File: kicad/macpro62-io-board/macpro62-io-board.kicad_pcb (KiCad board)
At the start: 6 copper layers, 101 x 173.6 mm, 113 parts, among them J1 IOB-HS1 MCIO 124 RA <- CB J3 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, J11 C1 GPU DP L0 (4-lane), J12 C2 GPU DP L1 (4-lane), J13 C3 GPU DP L3 (2-lane), J14 C4 GPU DP L4 (2-lane), J15 C5 iGPU DDI-B, J16 C6 iGPU DDI-C, J2 DISPLAY-LINK MCIO 74 RA <- Fa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, J21 USB-A A1 10G, J22 USB-A A2 10G, J23 USB-A A3 10G, J24 USB-A A4 10G, J25 ETH1 i226-V 2.5GbE (roomy fra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, J26 ETH2 rev B AQC107 10GbE (DNP 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, J27 HDMI (GPU link 2 via TDP158), J28 Stock audio module connector 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, J29 Speaker 2P (stock lead; pitch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, J3 Stock PSU DC-out 12P (UNCONFI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, J30 Optional stock/remote power b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, J31 I/O-wall (821-2222) flex ZIF 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, J4 Stock PSU signal 6P (UNCONFIR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, J5 PSU pass-through -> BP J2 (12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, J6 IOB-LINK GH15 <- BP J6, SW1 Power button on the IOB behin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, SW2 DIAG button, U1 TPS65994AD PD #1 (C1, C2), U11 TUSB1046A C1 alt-mode mux/red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, U12 TUSB1046A C2 alt-mode mux/red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, U13 TUSB1046A C3 alt-mode mux/red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, U14 TUSB1046A C4 alt-mode mux/red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, U15 TUSB1046A C5 alt-mode mux/red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, U16 TUSB1046A C6 alt-mode mux/red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, U2 TPS65994AD PD #2 (C3, C4), U21 TUSB1002A A1 10G redriver, U22 TUSB1002A A2 10G redriver, U23 TUSB1002A A3 10G redriver, U24 TUSB1002A A4 10G redriver, U25 USB-A A1 VBUS switch 1.5 A (S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, U26 USB-A A2 VBUS switch 1.5 A (S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, U27 USB-A A3 VBUS switch 1.5 A (S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, U28 USB-A A4 VBUS switch 1.5 A (S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, U3 TPS65994AD PD #3 (C5, C6), U30 Hall A (DRV5032 class) - posi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, U31 Hall B (DRV5032 class) - posi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, U32 CH334R hub H1b (C4-C6 + codec), U33 CH334R hub H2 (A1-A4) <- IOB-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, U34 CH334R hub H1a (C1-C3 + H1b) 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, U4 PD #1 config SPI flash (W25Q8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, U40 TPS259824ON eFuse 12 V in (15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, U41 TPS56C215 5V_C buck (USB-C VB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, U42 TPS56C215 5V_A buck (USB-A VB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, U43 TLV62585 3V3 (3 A) from 5V_SYS, U50 i226-V 2.5GbE (PCIe x1 from H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, U51 i226-V NVM SPI flash (size pe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, U6 PD #2 config SPI flash, U60 TDP158 HDMI 2.0 retimer (GPU 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, U61 1V1 LDO (TDP158 core), U7 PD #3 config SPI flash, U70 C-Media CM108B USB audio code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, U71 PAM8302A mono class-D 2.5 W (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, U80 TLC59116 16-ch I2C LED driver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, U81 LIS2DH12 accelerometer (rotat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, U82 BL24C64A IOB ID EEPROM @0x51, U83 TCA9517 I2C buffer (I2C_SYS <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, U84 74LVC1G07 PD_INT -> IOB_INT_N, Y1 12 MHz hub crystal, Y2 12 MHz hub crystal, Y3 12 MHz hub crystal, Y4 25 MHz (i226-V), Y5 12 MHz (CM108B)

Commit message: I/O board: second 2.5GbE (2x i226-V, HR913790A set back), ETH2 plate opening, CPU link pinout v0.2
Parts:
- added L45: i226 #2 SVR inductor, MP62_IO:L_1008_2520Metric, B.Cu at (113.0, 101.5)
- added U52: i226-V #2 2.5GbE (PCIe x1 from HS1 k14, PCH RP4), MP62_IO:MP62_Intel_i226V_QFN-56_7x7_P0.4_PLACEHOLDER, B.Cu at (113.0, 108.0)
- added U53: i226-V #2 NVM SPI flash, MP62_IO:SOIC-8_3.9x4.9mm_P1.27mm, B.Cu at (121.5, 113.5)
- added Y6: 25 MHz (i226-V #2), MP62_IO:Crystal_SMD_3225-4Pin_3.2x2.5mm, B.Cu at (113.0, 115.0)
- J25: value ETH1 i226-V 2.5GbE (roomy frame side) -> ETH1 i226-V #1 2.5GbE, HR913790A (face behind the frame plane); footprint MP62_IO:MP62_RJ45_Mag_2G5_Vertical_PLACEHOLDER -> MP62_IO:MP62_RJ45_HanRun_HR913790A_Vertical_2G5
- J26: value ETH2 rev B AQC107 10GbE (DNP rev A; frame slot 15.6: jack set back) -> ETH2 i226-V #2 2.5GbE, HR913790A; H-side frame slot 15.6 x 13.0 < body 16.2 x 17.0: jack set back behind the frame, plu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; footprint MP62_IO:MP62_RJ45_Mag_2G5_Vertical_PLACEHOLDER -> MP62_IO:MP62_RJ45_HanRun_HR913790A_Vertical_2G5
- moved Y2 6.52 mm to (88.0, 104.5)

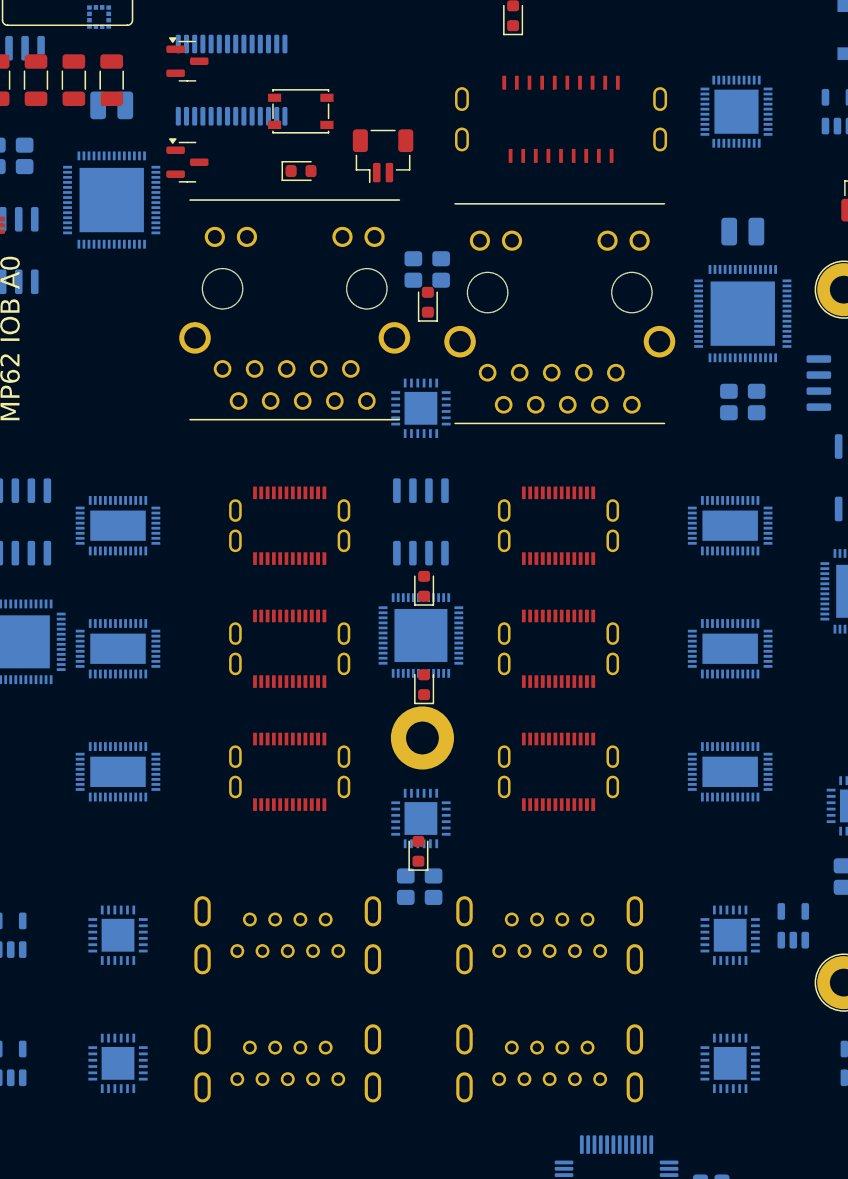
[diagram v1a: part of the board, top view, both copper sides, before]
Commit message: I/O plate: flex retraced from flat scan, flush inner face, LED pockets, measured 16.5-18 mm gap; connector re-grid
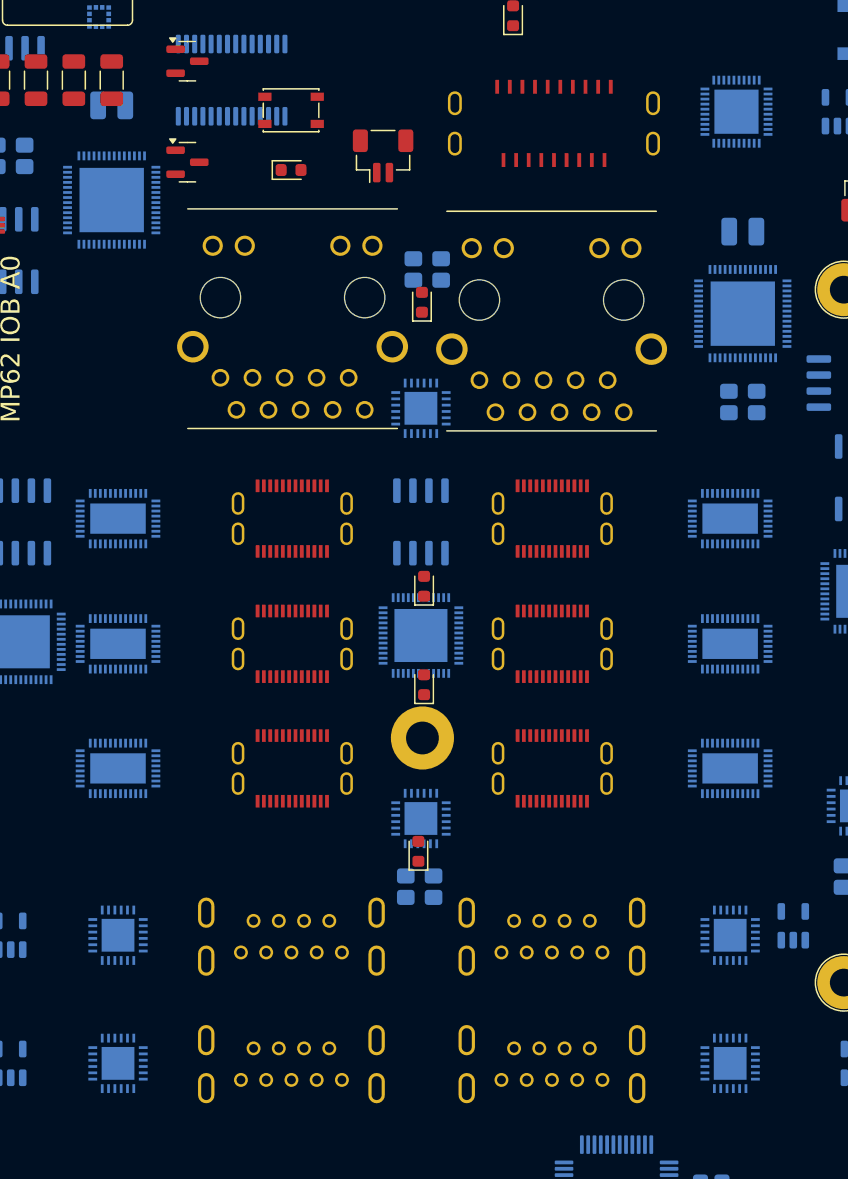
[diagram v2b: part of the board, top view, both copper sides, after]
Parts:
- D20: value Power/sleep LED (white) under button cap -> DNP with the stock flex (its 2 button LEDs light the cap via J31); power/sleep LED only without the flex
- D21: value Light-pipe LED: HDMI label -> Light-pipe LED: HDMI label - DNP with the stock flex (its own LEDs light the icon pads via J31)
- D22: value Light-pipe LED: ETH icon -> Light-pipe LED: ETH icon - DNP with the stock flex (its own LEDs light the icon pads via J31)
- D23: value Light-pipe LED: USB-C icon upper -> Light-pipe LED: USB-C icon upper - DNP with the stock flex (its own LEDs light the icon pads via J31)
- D24: value Light-pipe LED: USB-C icon lower -> Light-pipe LED: USB-C icon lower - DNP with the stock flex (its own LEDs light the icon pads via J31)
- D25: value Light-pipe LED: USB icon -> Light-pipe LED: USB icon - DNP with the stock flex (its own LEDs light the icon pads via J31)
- D26: value Light-pipe LED: audio icons -> Light-pipe LED: audio icons - DNP with the stock flex (its own LEDs light the icon pads via J31)
- J11: value C1 GPU DP L0 (4-lane) -> C1 GPU DP L0 (4-lane); FG-ST-C-24P-VT-SMT-15.0 C51911913 H15.0 on +2.9 port riser (mouth 17.90)
- J12: value C2 GPU DP L1 (4-lane) -> C2 GPU DP L1 (4-lane); FG-ST-C-24P-VT-SMT-15.0 C51911913 H15.0 on +2.9 port riser (mouth 17.90)
- J13: value C3 GPU DP L3 (2-lane) -> C3 GPU DP L3 (2-lane); FG-ST-C-24P-VT-SMT-15.0 C51911913 H15.0 on +2.9 port riser (mouth 17.90)
- J14: value C4 GPU DP L4 (2-lane) -> C4 GPU DP L4 (2-lane); FG-ST-C-24P-VT-SMT-15.0 C51911913 H15.0 on +2.8 port riser (mouth 17.82)
- J15: value C5 iGPU DDI-B -> C5 iGPU DDI-B; FG-ST-C-24P-VT-SMT-15.0 C51911913 H15.0 on +2.8 port riser (mouth 17.82)
- J16: value C6 iGPU DDI-C -> C6 iGPU DDI-C; FG-ST-C-24P-VT-SMT-15.0 C51911913 H15.0 on +2.8 port riser (mouth 17.82)
- J21: value USB-A A1 10G -> USB-A A1 10G; KH-3.0AF180WJ-15JB C2979045 L15.0 on +2.5 port riser (mouth 17.49)
- J22: value USB-A A2 10G -> USB-A A2 10G; KH-3.0AF180WJ-15JB C2979045 L15.0 on +2.5 port riser (mouth 17.49)
- J23: value USB-A A3 10G -> USB-A A3 10G; KH-3.0AF180WJ-15JB C2979045 L15.0 on +2.4 port riser (mouth 17.38)
- J24: value USB-A A4 10G -> USB-A A4 10G; KH-3.0AF180WJ-15JB C2979045 L15.0 on +2.4 port riser (mouth 17.38)
- J25: value ETH1 i226-V #1 2.5GbE, HR913790A (face behind the frame plane) -> ETH1 i226-V #1 2.5GbE. HR913790A (16.9) TOO TALL for D0 18: face must be <= 13.6 -> non-magnetic vertical RJ45 <= 13.0 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
- J26: value ETH2 i226-V #2 2.5GbE, HR913790A; H-side frame slot 15.6 x 13.0 < body 16.2 x 17.0: jack set back behind the frame, plu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 -> ETH2 i226-V #2 2.5GbE. HR913790A (16.9) TOO TALL for D0 18: face must be <= 13.7 (behind the frame) -> non-magnetic ver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
- J27: value HDMI (GPU link 2 via TDP158) -> HDMI (GPU link 2 via TDP158); vertical H15 (JLC C9900153431, verify shell <= 15.4 x 5.6) on +2.2 port riser (mouth 17.2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
- SW1: value Power button on the IOB behind the plate opening (printed cap); stock button is NOT on the stock IOB -> DNP with the stock 821-2222-A flex (its dome switch is the power button, via J31); fit only without the flex
- moved J26 0.88 mm to (97.9, 108.6)
- moved D20 0.79 mm to (77.2, 96.6)
- moved SW1 0.77 mm to (77.2, 91.9)
- moved J11 0.74 mm to (97.9, 124.2)
- moved J25 0.72 mm to (77.3, 108.4)
- moved J27 0.65 mm to (98.0, 92.9)
- moved J12 0.63 mm to (97.9, 134.2)
- moved J14 0.60 mm to (77.3, 124.2)
- moved U11 0.56 mm to (112.0, 124.2)
- moved U14 0.56 mm to (63.5, 124.2)
- moved J13 0.56 mm to (97.9, 144.0)
- moved D22 0.47 mm to (87.6, 107.1)
- moved J15 0.44 mm to (77.3, 134.2)
- moved U12 0.39 mm to (112.0, 134.2)
- moved U15 0.39 mm to (63.5, 134.2)
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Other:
- board text added: "All ports are VERTICAL (mating axis normal to the board); the plate is curved with no lands (stock flex must lie flat), mouths flush at the outboard edge (plan 4.4/4.7)."
- board text added: "D0 = 18.0 crown / 16.5 edge: USB-C/USB-A/HDMI need 17.2-17.9 board-to-mouth -> port risers (+2.2..2.9) under 15.0 parts; RJ45 face <= 13.6 (plan 4.7.4)."
- board text added: "Port grid (stock flex cut-outs, scan 2026-10-02): USB-C Xb 43.09 / 63.69, Y 75.76 / 65.84 / 55.97; USB-A 43.12 / 63.76, Y 42.64 / 32.54; RJ45 (43.15,91.41)/(63.67,91.60); HDMI (42.96,107.07); button (63.79,108.11)."
- board text removed: "All ports are VERTICAL (mating axis normal to the board) like stock; plate openings follow the connectors; tilt (~1-3 deg est.) is taken up by the plate (plan 4.4)."
- board text removed: "Port grid: columns Xb 42.6 / 63.9; USB-C rows Y 75.2 / 65.45 / 55.7; USB-A rows 42.75 / 32.6; RJ45 Y ~92; HDMI (42.4,107.4); button (63.0,108.0)."

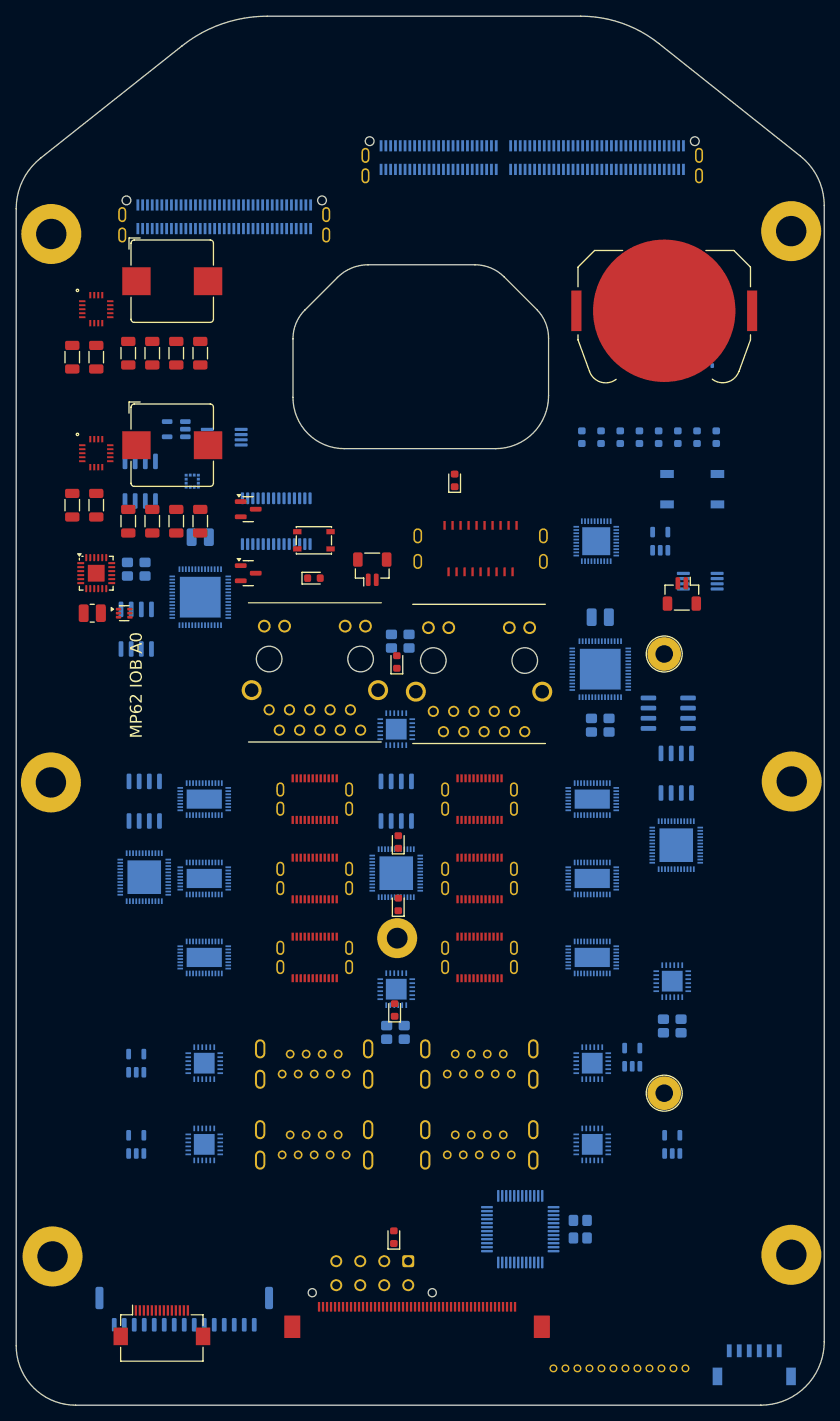
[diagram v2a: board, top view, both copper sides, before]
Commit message: I/O: tilted port risers (USB-C/USB-A/HDMI, DF40 + flex jumpers), low RJ45 + V24P05S magnetics, fan+AirPort CONN_C at stock position, ASM1182e lane share; plate R=111
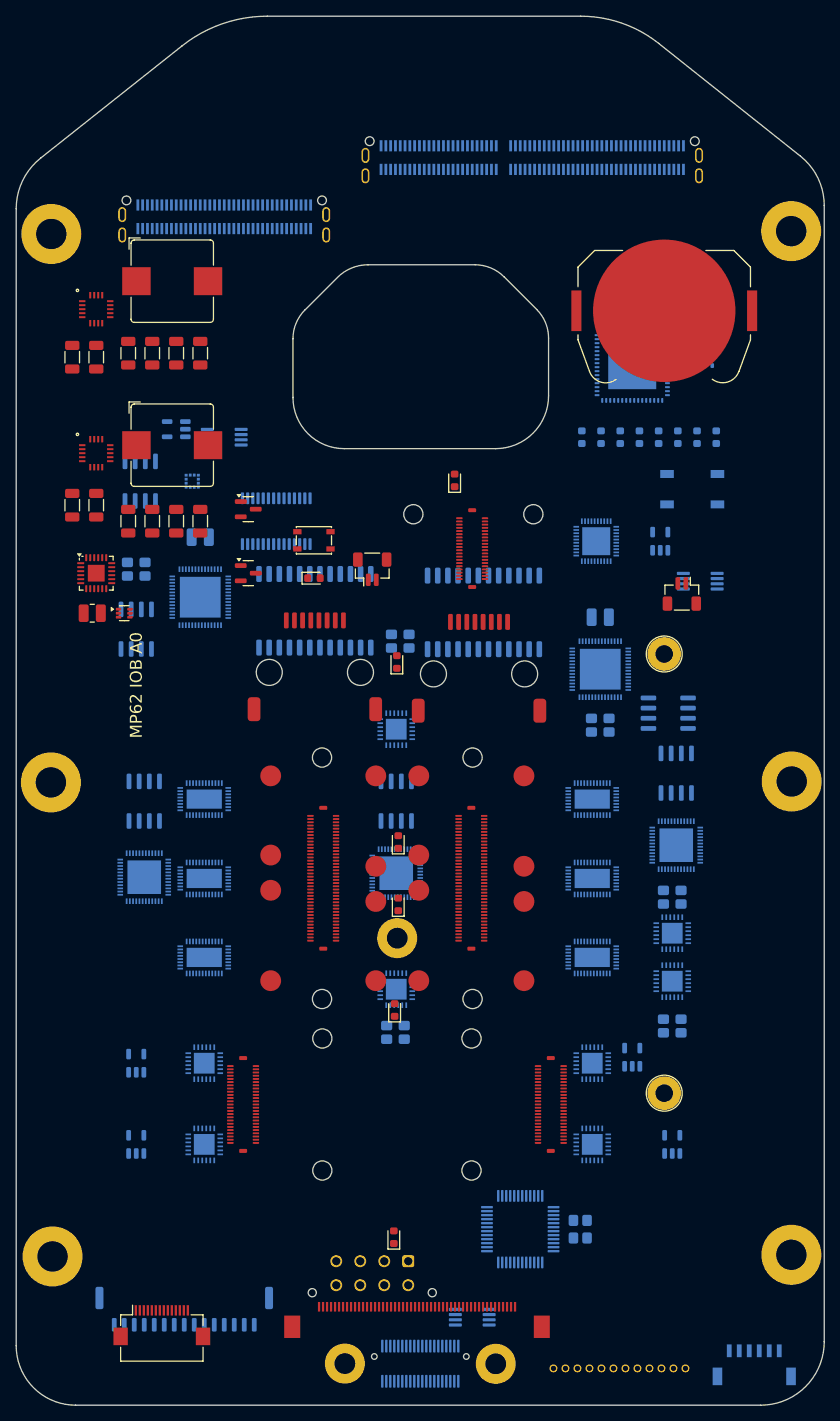
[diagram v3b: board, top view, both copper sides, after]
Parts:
- removed J11: C1 GPU DP L0 (4-lane); FG-ST-C-24P-VT-SMT-15.0 C51911913 H1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, MP62_IO:MP62_USB_C_24P_Vertical_PLACEHOLDER
- removed J12: C2 GPU DP L1 (4-lane); FG-ST-C-24P-VT-SMT-15.0 C51911913 H1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, MP62_IO:MP62_USB_C_24P_Vertical_PLACEHOLDER
- removed J13: C3 GPU DP L3 (2-lane); FG-ST-C-24P-VT-SMT-15.0 C51911913 H1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, MP62_IO:MP62_USB_C_24P_Vertical_PLACEHOLDER
- removed J14: C4 GPU DP L4 (2-lane); FG-ST-C-24P-VT-SMT-15.0 C51911913 H1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, MP62_IO:MP62_USB_C_24P_Vertical_PLACEHOLDER
- removed J15: C5 iGPU DDI-B; FG-ST-C-24P-VT-SMT-15.0 C51911913 H15.0 on +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, MP62_IO:MP62_USB_C_24P_Vertical_PLACEHOLDER
- removed J16: C6 iGPU DDI-C; FG-ST-C-24P-VT-SMT-15.0 C51911913 H15.0 on +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, MP62_IO:MP62_USB_C_24P_Vertical_PLACEHOLDER
- removed J21: USB-A A1 10G; KH-3.0AF180WJ-15JB C2979045 L15.0 on +2.5 por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, MP62_IO:MP62_USB_A3_9P_Vertical_PLACEHOLDER
- removed J22: USB-A A2 10G; KH-3.0AF180WJ-15JB C2979045 L15.0 on +2.5 por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, MP62_IO:MP62_USB_A3_9P_Vertical_PLACEHOLDER
- removed J23: USB-A A3 10G; KH-3.0AF180WJ-15JB C2979045 L15.0 on +2.4 por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, MP62_IO:MP62_USB_A3_9P_Vertical_PLACEHOLDER
- removed J24: USB-A A4 10G; KH-3.0AF180WJ-15JB C2979045 L15.0 on +2.4 por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, MP62_IO:MP62_USB_A3_9P_Vertical_PLACEHOLDER
- removed J27: HDMI (GPU link 2 via TDP158); vertical H15 (JLC C9900153431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, MP62_IO:MP62_HDMI_A_Vertical_PLACEHOLDER
- added H14: CONN_C threaded standoff (stock position 41.06, 5.17; threa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, MP62_IO:MP62_Frame_Standoff_M2_SMT_PLACEHOLDER, B.Cu at (99.9, 194.8)
- added H15: CONN_C threaded standoff (stock position 59.92, 5.20; threa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, MP62_IO:MP62_Frame_Standoff_M2_SMT_PLACEHOLDER, B.Cu at (81.1, 194.8)
- added H21: RC_H cradle M2 screw (printed PA12 wedge cradle), MP62_IO:MP62_Cradle_Screw_M2_NPTH, F.Cu at (97.0, 149.2)
- added H22: RC_H cradle M2 screw (printed PA12 wedge cradle), MP62_IO:MP62_Cradle_Screw_M2_NPTH, F.Cu at (97.0, 119.0)
- added H23: RC_O cradle M2 screw (printed PA12 wedge cradle), MP62_IO:MP62_Cradle_Screw_M2_NPTH, F.Cu at (78.2, 149.2)
- added H24: RC_O cradle M2 screw (printed PA12 wedge cradle), MP62_IO:MP62_Cradle_Screw_M2_NPTH, F.Cu at (78.2, 119.0)
- added H25: RA_H cradle M2 screw (printed PA12 wedge cradle), MP62_IO:MP62_Cradle_Screw_M2_NPTH, F.Cu at (96.9, 170.7)
- added H26: RA_H cradle M2 screw (printed PA12 wedge cradle), MP62_IO:MP62_Cradle_Screw_M2_NPTH, F.Cu at (96.9, 154.2)
- added H27: RA_O cradle M2 screw (printed PA12 wedge cradle), MP62_IO:MP62_Cradle_Screw_M2_NPTH, F.Cu at (78.3, 170.7)
- added H28: RA_O cradle M2 screw (printed PA12 wedge cradle), MP62_IO:MP62_Cradle_Screw_M2_NPTH, F.Cu at (78.3, 154.2)
- added H29: RH cradle M2 screw (printed PA12 wedge cradle), MP62_IO:MP62_Cradle_Screw_M2_NPTH, F.Cu at (104.6, 88.6)
- added H30: RH cradle M2 screw (printed PA12 wedge cradle), MP62_IO:MP62_Cradle_Screw_M2_NPTH, F.Cu at (89.6, 88.6)
- added J7: CONN_C fan + AirPort 2x20 @0.5 (stock press B2B). DF12-40DS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, MP62_IO:MP62_Hirose_DF12-40DS-0.5V_PLACEHOLDER, B.Cu at (90.5, 194.8)
- added JR1: RC_H riser link (C, ports C1/C2/C3, tilt -5.27 deg): DF40C-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, MP62_IO:MP62_Hirose_DF40C-80DS-0.4V_PLACEHOLDER, F.Cu at (96.9, 134.1)
- added JR2: RC_O riser link (C, ports C4/C5/C6, tilt 5.47 deg): DF40C-8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, MP62_IO:MP62_Hirose_DF40C-80DS-0.4V_PLACEHOLDER, F.Cu at (78.4, 134.1)
- added JR3: RA_H riser link (A, ports A1/A2, tilt -5.25 deg): DF40C-50D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, MP62_IO:MP62_Hirose_DF40C-50DS-0.4V_PLACEHOLDER, F.Cu at (106.8, 162.4)
- added JR4: RA_O riser link (A, ports A3/A4, tilt 5.51 deg): DF40C-50DS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, MP62_IO:MP62_Hirose_DF40C-50DS-0.4V_PLACEHOLDER, F.Cu at (68.4, 162.4)
- added JR5: RH riser link (HDMI, ports HDMI, tilt -5.33 deg): DF40C-40D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, MP62_IO:MP62_Hirose_DF40C-40DS-0.4V_PLACEHOLDER, F.Cu at (97.0, 92.9)
- added PG1: RC_H pogo VBUS_C3, working height 5.94, MP62_IO:MP62_Pogo_SMD_D2.0_PLACEHOLDER, F.Cu at (103.5, 146.9)
- added PG10: RC_O pogo VBUS_C3, working height 7.14, MP62_IO:MP62_Pogo_SMD_D2.0_PLACEHOLDER, F.Cu at (84.9, 121.3)
- added PG11: RC_O pogo VBUS_C2, working height 5.88, MP62_IO:MP62_Pogo_SMD_D2.0_PLACEHOLDER, F.Cu at (71.8, 135.6)
- added PG12: RC_O pogo VBUS_C2, working height 7.14, MP62_IO:MP62_Pogo_SMD_D2.0_PLACEHOLDER, F.Cu at (84.9, 132.6)
- added PG13: RC_O pogo VBUS_C1, working height 5.88, MP62_IO:MP62_Pogo_SMD_D2.0_PLACEHOLDER, F.Cu at (71.8, 146.9)
- added PG14: RC_O pogo VBUS_C1, working height 7.14, MP62_IO:MP62_Pogo_SMD_D2.0_PLACEHOLDER, F.Cu at (84.9, 146.9)
- added PG15: RC_O pogo GND, working height 5.88, MP62_IO:MP62_Pogo_SMD_D2.0_PLACEHOLDER, F.Cu at (71.8, 131.2)
- added PG16: RC_O pogo GND, working height 7.14, MP62_IO:MP62_Pogo_SMD_D2.0_PLACEHOLDER, F.Cu at (84.9, 137.0)
- added PG2: RC_H pogo VBUS_C3, working height 7.15, MP62_IO:MP62_Pogo_SMD_D2.0_PLACEHOLDER, F.Cu at (90.3, 146.9)
- added PG3: RC_H pogo VBUS_C2, working height 5.94, MP62_IO:MP62_Pogo_SMD_D2.0_PLACEHOLDER, F.Cu at (103.5, 132.6)
- added PG4: RC_H pogo VBUS_C2, working height 7.15, MP62_IO:MP62_Pogo_SMD_D2.0_PLACEHOLDER, F.Cu at (90.3, 135.6)
- added PG5: RC_H pogo VBUS_C1, working height 5.94, MP62_IO:MP62_Pogo_SMD_D2.0_PLACEHOLDER, F.Cu at (103.5, 121.3)
- added PG6: RC_H pogo VBUS_C1, working height 7.15, MP62_IO:MP62_Pogo_SMD_D2.0_PLACEHOLDER, F.Cu at (90.3, 121.3)
- added PG7: RC_H pogo GND, working height 5.94, MP62_IO:MP62_Pogo_SMD_D2.0_PLACEHOLDER, F.Cu at (103.5, 137.0)
- added PG8: RC_H pogo GND, working height 7.15, MP62_IO:MP62_Pogo_SMD_D2.0_PLACEHOLDER, F.Cu at (90.3, 131.2)
- added PG9: RC_O pogo VBUS_C3, working height 5.88, MP62_IO:MP62_Pogo_SMD_D2.0_PLACEHOLDER, F.Cu at (71.8, 121.3)
- added T1: ETH1 2.5G magnetics JASN V24P05S C2827281 (B side, clear of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, MP62_IO:MP62_JASN_V24P05S_SMD-24P_15.1x7.1_PLACEHOLDER, B.Cu at (77.3, 100.7)
- added T2: ETH2 2.5G magnetics JASN V24P05S C2827281 (B side, clear of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, MP62_IO:MP62_JASN_V24P05S_SMD-24P_15.1x7.1_PLACEHOLDER, B.Cu at (98.4, 100.9)
- added U35: CH334R hub H3 on H2 port 4: A4 + Bluetooth USB2 (J7) + 2 sp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, MP62_IO:MP62_WCH_CH334R_QFN-24_4x4_P0.5_PLACEHOLDER, B.Cu at (122.0, 141.0)
- added U90: EMC2101 fan controller @0x4C on I2C_SYS: PWM + TACH to J7, 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, MP62_IO:MSOP-8_3x3mm_P0.65mm, B.Cu at (97.0, 189.0)
- added U91: ASM1182e PCIe Gen2 switch: up = HS1 k14 lane (was i226 #2),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, MP62_IO:MP62_ASMedia_ASM1182e_QFN-64_9x9_P0.5_PLACEHOLDER, B.Cu at (117.0, 70.0)
- added Y7: 12 MHz hub crystal (H3), MP62_IO:Crystal_SMD_3225-4Pin_3.2x2.5mm, B.Cu at (122.0, 136.5)
- J25: value ETH1 i226-V #1 2.5GbE. HR913790A (16.9) TOO TALL for D0 18: face must be <= 13.6 -> non-magnetic vertical RJ45 <= 13.0 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 -> ETH1 i226-V #1: ZJLQ-RJ45-SMD-PCB125-8P8C C55547809 (no magnetics, height <= 13.0 VERIFY) - D-IO15; footprint MP62_IO:MP62_RJ45_HanRun_HR913790A_Vertical_2G5 -> MP62_IO:MP62_RJ45_Vertical_SMD_NoMag_PLACEHOLDER
- J26: value ETH2 i226-V #2 2.5GbE. HR913790A (16.9) TOO TALL for D0 18: face must be <= 13.7 (behind the frame) -> non-magnetic ver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 -> ETH2 i226-V #2: ZJLQ-RJ45-SMD-PCB125-8P8C C55547809 (no magnetics, height <= 13.0 VERIFY) - D-IO15; footprint MP62_IO:MP62_RJ45_HanRun_HR913790A_Vertical_2G5 -> MP62_IO:MP62_RJ45_Vertical_SMD_NoMag_PLACEHOLDER
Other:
- board text added: "RA_H riser -5.2 deg"
- board text added: "RA_O riser 5.5 deg"
- board text added: "RC_H riser -5.3 deg"
- board text added: "RC_O riser 5.5 deg"
- board text added: "RH riser -5.3 deg"
